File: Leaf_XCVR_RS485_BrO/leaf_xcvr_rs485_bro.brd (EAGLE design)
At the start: 22.5 x 31.7 mm, 11 parts, among them U1 RS485_XCVR_SN65HVD178X

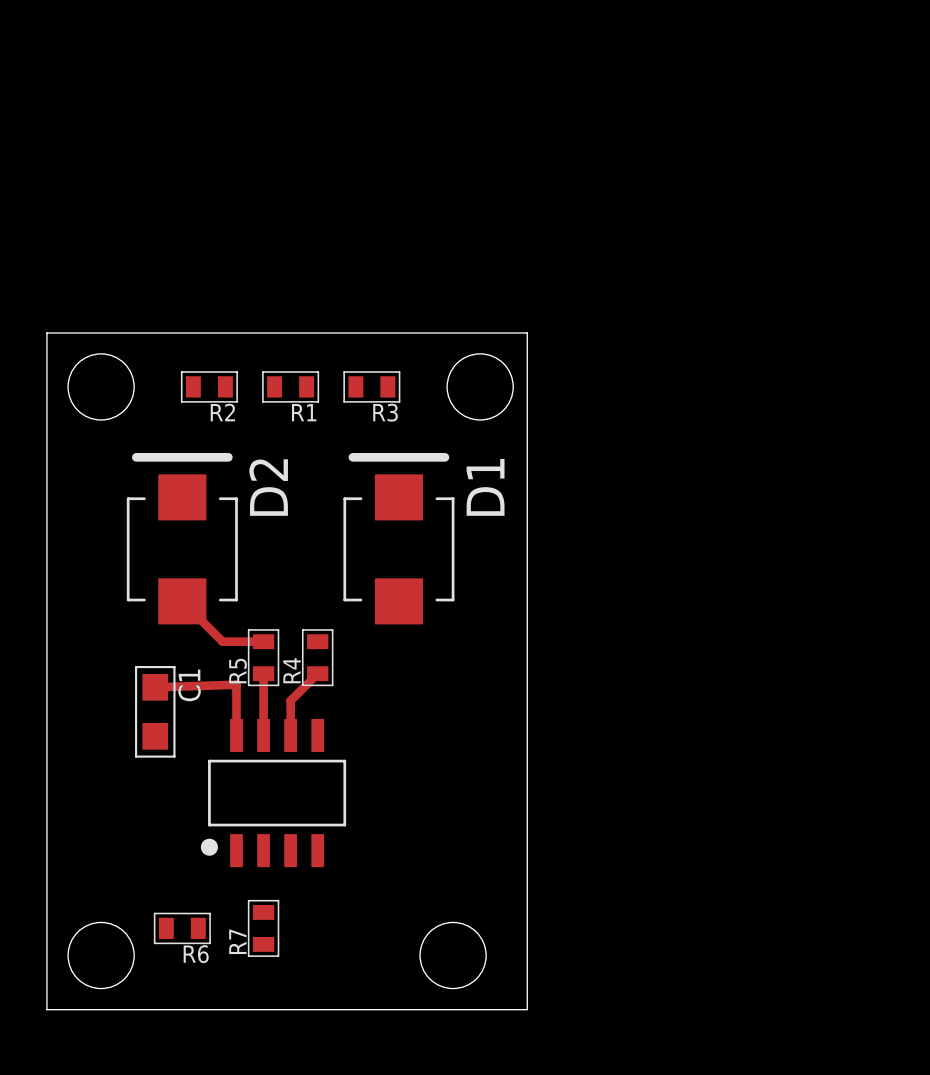
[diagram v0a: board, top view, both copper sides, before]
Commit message: new xcvr board for mockups
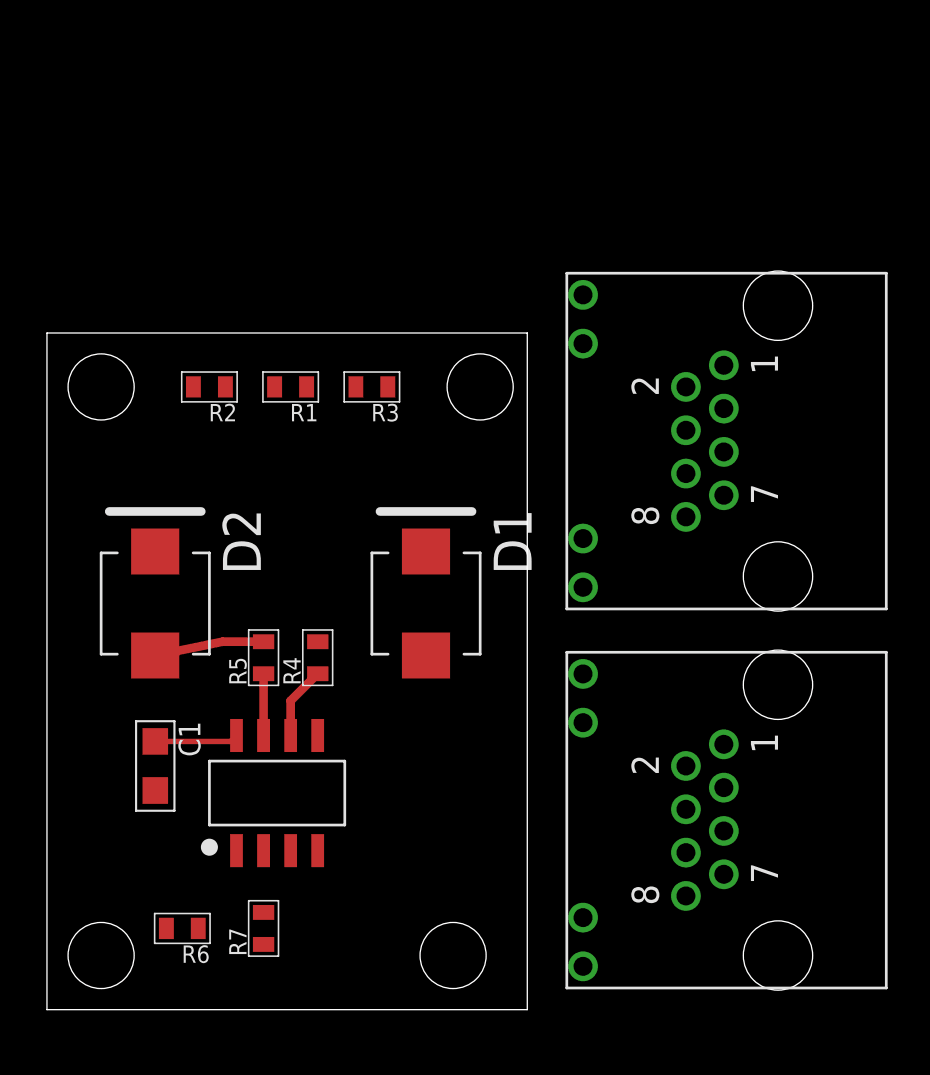
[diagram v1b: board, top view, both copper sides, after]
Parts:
- added J$1, J$2: (no value), stepOSP:RJHSE-5085
- moved D1 2.84 mm to (17.8, 19.1)
- moved D2 2.84 mm to (5.08, 19.1)
- moved C1 2.54 mm to (5.08, 11.4)
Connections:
- removed net N$3: C1.P$1, U1.8
- new net +3V3: C1.P$1, R2.P$2, R6.P$2, U1.8
- new net GND: C1.P$2, D1.P$1, D2.P$1, R3.P$1, R7.P$1, U1.5
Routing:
- net N$3: track 6.19 -> 0.00 mm
- net +3V3: track 0.00 -> 3.93 mm
- net N$7: track 4.59 -> 5.15 mm
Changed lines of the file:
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@@
 </autorouter>
 <elements>
-<element name="C1" library="stepOSP" package="0805" value="" x="5.08" y="13.97" rot="R270"/>
-<element name="D1" library="leaf" package="DO-214AA_LITTELFUSE" value="TVS_DO-214AA" x="16.51" y="21.59" rot="R270"/>
-<element name="D2" library="leaf" package="DO-214AA_LITTELFUSE" value="TVS_DO-214AA" x="6.35" y="21.59" rot="R270"/>
+<element name="C1" library="stepOSP" package="0805" value="" x="5.08" y="11.43" rot="R270"/>
+<element name="D1" library="leaf" package="DO-214AA_LITTELFUSE" value="TVS_DO-214AA" x="17.78" y="19.05" rot="R270"/>
+<element name="D2" library="leaf" package="DO-214AA_LITTELFUSE" value="TVS_DO-214AA" x="5.08" y="19.05" rot="R270"/>
 <element name="R1" library="stepOSP" package="0603" value="" x="11.43" y="29.21" rot="R180"/>
 <element name="R2" library="stepOSP" package="0603" value="" x="7.62" y="29.21" rot="R180"/>
@@
 <element name="R7" library="stepOSP" package="0603" value="" x="10.16" y="3.81" rot="R90"/>
 <element name="U1" library="leaf" package="SOIC_08_TI" value="RS485_XCVR_SN65HVD178X" x="8.89" y="10.16"/>
+<element name="J$1" library="stepOSP" package="RJHSE-5085" value="" x="34.29" y="2.54" rot="R90"/>
+<element name="J$2" library="stepOSP" package="RJHSE-5085" value="" x="34.29" y="20.32" rot="R90"/>
 </elements>
 <signals>
-<signal name="N$3">
-<contactref element="U1" pad="8"/>
-<contactref element="C1" pad="P$1"/>
-<wire x1="5.08" y1="15.12" x2="8.89" y2="15.24" width="0.4064" layer="1"/>
-<wire x1="8.89" y1="15.24" x2="8.89" y2="12.86" width="0.4064" layer="1"/>
-</signal>
 <signal name="N$1">
 <contactref element="U1" pad="6"/>
@@
 <wire x1="12.7" y1="17.26" x2="12.18" y2="29.21" width="0" layer="19" extent="1-1"/>
 <wire x1="14.49" y1="29.21" x2="12.7" y2="17.26" width="0" layer="19" extent="1-1"/>
-<wire x1="16.51" y1="19.1516" x2="14.49" y2="29.21" width="0" layer="19" extent="1-1"/>
+<wire x1="17.78" y1="16.6116" x2="14.49" y2="29.21" width="0" layer="19" extent="1-1"/>
 </signal>
 <signal name="N$7">
@@
 <contactref element="R2" pad="P$1"/>
 <wire x1="10.16" y1="17.26" x2="8.2416" y2="17.26" width="0.4064" layer="1"/>
-<wire x1="8.2416" y1="17.26" x2="6.35" y2="19.1516" width="0.4064" layer="1"/>
+<wire x1="8.2416" y1="17.26" x2="5.08" y2="16.6116" width="0.4064" layer="1"/>
 <wire x1="8.37" y1="29.21" x2="10.68" y2="29.21" width="0" layer="19" extent="1-1"/>
-<wire x1="6.35" y1="19.1516" x2="8.37" y2="29.21" width="0" layer="19" extent="1-1"/>
+<wire x1="5.08" y1="16.6116" x2="8.37" y2="29.21" width="0" layer="19" extent="1-1"/>
 </signal>
 <signal name="N$8">
@@
 <contactref element="U1" pad="4"/>
 </signal>
+<signal name="+3V3">
+<contactref element="R6" pad="P$2"/>
+<contactref element="R2" pad="P$2"/>
+<contactref element="C1" pad="P$1"/>
+<contactref element="U1" pad="8"/>
+<wire x1="5.08" y1="12.58" x2="8.61" y2="12.58" width="0.254" layer="1"/>
+<wire x1="8.61" y1="12.58" x2="8.89" y2="12.86" width="0.254" layer="1"/>
+<wire x1="8.89" y1="12.86" x2="6.87" y2="29.21" width="0" layer="19" extent="1-1"/>
+<wire x1="5.6" y1="3.81" x2="5.08" y2="12.58" width="0" layer="19" extent="1-1"/>
+</signal>
+<signal name="GND">
+<contactref element="C1" pad="P$2"/>
+<contactref element="D2" pad="P$1"/>
+<contactref element="D1" pad="P$1"/>
+<contactref element="R3" pad="P$1"/>
+<contactref element="R7" pad="P$1"/>
+<contactref element="U1" pad="5"/>
+<wire x1="17.78" y1="21.4884" x2="15.99" y2="29.21" width="0" layer="19" extent="1-1"/>
+<wire x1="5.08" y1="21.4884" x2="17.78" y2="21.4884" width="0" layer="19" extent="1-1"/>
+<wire x1="5.08" y1="10.28" x2="5.08" y2="21.4884" width="0" layer="19" extent="1-1"/>
+<wire x1="12.7" y1="12.86" x2="5.08" y2="10.28" width="0" layer="19" extent="1-1"/>
+<wire x1="10.16" y1="3.06" x2="12.7" y2="12.86" width="0" layer="19" extent="1-1"/>
+</signal>
 </signals>

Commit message: updating rs485 breakout
added a few new connectors and trying out some new designs
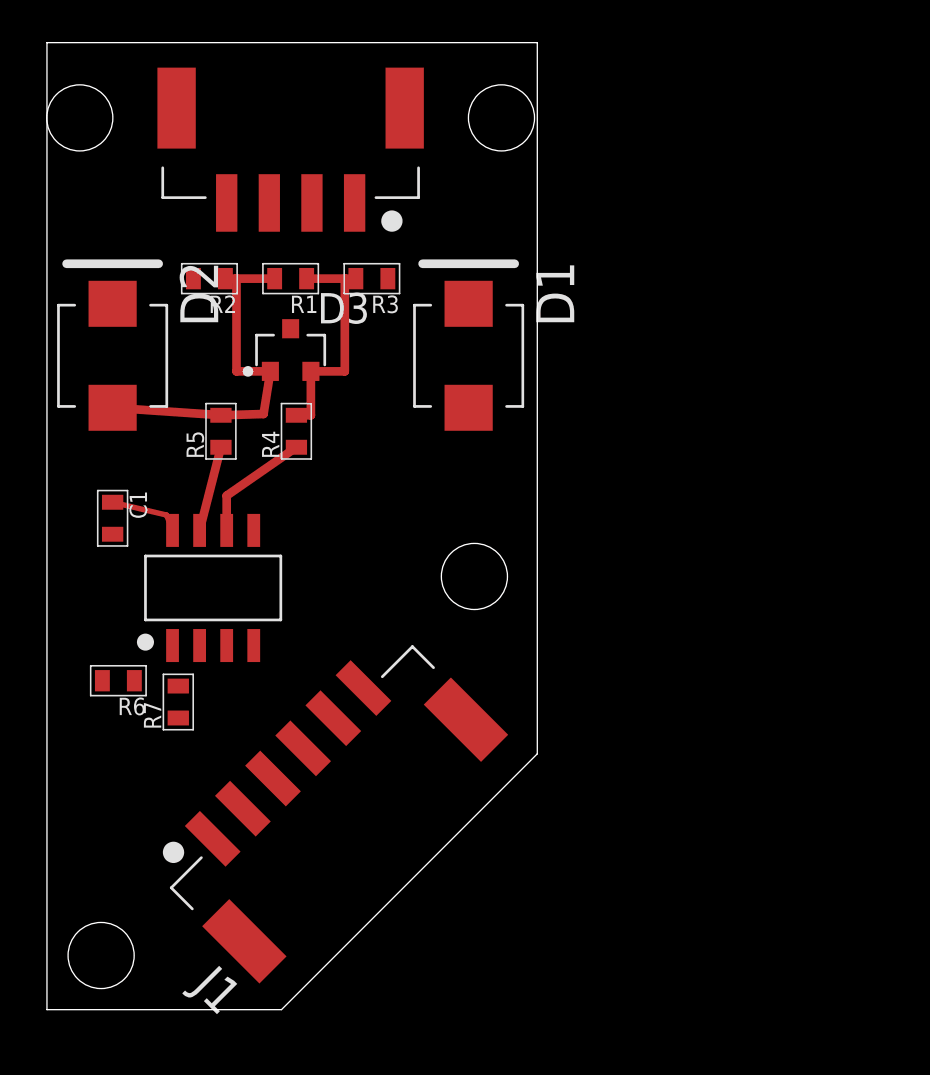
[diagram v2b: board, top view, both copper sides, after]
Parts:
- removed J$1, J$2: (no value), stepOSP:RJHSE-5085
- added D3: TVS_SOT-23, leaf:SOT-23_ONSEMI
- added J1: CONN_6X1_JST_PA, leaf:CONN_6X1_JST_PA
- added J2: CONN_4X1_JST_PA, leaf:CONN_4X1_JST_PA
- C1: device stepOSP:0805 -> stepOSP:0603
- moved R6 12.0 mm to (3.35, 15.4)
- moved C1 11.8 mm to (3.08, 23.1)
- moved D1 11.8 mm to (19.8, 30.7)
- moved D2 11.8 mm to (3.08, 30.7)
- moved R7 11.3 mm to (6.16, 14.4)
- moved R5 10.8 mm to (8.16, 27.1)
- moved R4 10.7 mm to (11.7, 27.1)
- moved U1 10.1 mm to (5.89, 19.8)
- moved R1 5.08 mm to (11.4, 34.3)
- moved R2 5.08 mm to (7.62, 34.3)
- moved R3 5.08 mm to (15.2, 34.3)
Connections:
- new net N$4: J1.2
- new net N$5: J2.4
- net +3V3: now also J1.3
- net GND: now also D3.3, J1.1, J2.1
- net N$10: now also J1.6
- net N$6: now also D3.2, J2.2
- net N$7: now also D3.1, J2.3
- net N$8: now also J1.5
- net N$9: now also J1.4
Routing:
- net N$7: track 5.15 -> 17.5 mm
- net N$6: track 0.00 -> 11.0 mm
- net N$1: track 3.43 -> 5.61 mm
- net N$2: track 2.90 -> 4.03 mm
- net +3V3: track 3.93 -> 3.37 mm
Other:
- board size 22.5 x 31.7 mm -> 23 x 45.4 mm

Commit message: latest and greatest
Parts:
- J1: value CONN_6X1_JST_PA -> CONN_7X1_JST_PA; device leaf:CONN_6X1_JST_PA -> leaf:CONN_7X1_JST_PA
- moved D3 7.69 mm to (16.9, 25.6), turned to 315 degrees
- moved R4 5.83 mm to (14.7, 22.1), turned to 45 degrees
- moved R5 5.83 mm to (13.2, 24.1), turned to 45 degrees
- moved R2 5.50 mm to (12.3, 31.4), turned to 90 degrees
- moved R1 5.00 mm to (14.4, 30.3)
- moved D2 4.47 mm to (7.08, 28.7)
- moved C1 4.12 mm to (7.08, 22.1), turned to 225 degrees
- moved R3 3.39 mm to (16.7, 31.2), turned to 270 degrees
- moved U1 2.91 mm to (8.78, 20.1), turned to 315 degrees
- moved J1 2.40 mm to (20.0, 6.00)
- moved D1 2.24 mm to (21.8, 29.7)
- moved R6 2.24 mm to (4.35, 17.4), turned to 135 degrees
- moved J2 1.58 mm to (13.0, 46.8)
- moved R7 1.00 mm to (7.16, 14.4), turned to 135 degrees
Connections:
- removed net GND: C1.P$2, D1.P$1, D2.P$1, D3.3, J1.1, J2.1, R3.P$1, R7.P$1, U1.5
- removed net N$4: J1.2
- removed net N$5: J2.4
- new net GND1: C1.P$2, D1.P$1, D2.P$1, D3.3, J1.3, R3.P$1, R7.P$1, U1.5
- new net GND2: J1.1, J2.1
- new net V+: J1.2, J2.4
- net +3V3: now also J1.4; no longer J1.3
- net N$10: now also J1.7; no longer J1.6
- net N$8: now also J1.6; no longer J1.5
- net N$9: now also J1.5; no longer J1.4
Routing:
- net N$7: track 17.5 -> 0.00 mm
- net N$6: track 11.0 -> 0.00 mm
- net N$1: track 5.61 -> 0.00 mm
- net N$2: track 4.03 -> 0.00 mm
- net +3V3: track 3.37 -> 0.00 mm
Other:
- board size 23 x 45.4 mm -> 26 x 45 mm

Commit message: submission to OSHpark
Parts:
- added TP1, TP2, TP3, TP4, TP5, TP6, TP7, TP8, TP9: TP1, leaf:TP1
- added U$1: STEPS_LOGO, stepOSP:STEPS_LOGO
- C1: value (none) -> 0.1u
- R1: value (none) -> 120
- R4, R5: value (none) -> 10
- R6, R7: value (none) -> 3.3k
- moved D1 16.6 mm to (5.33, 27.8), turned to 0 degrees
- moved D2 6.82 mm to (5.33, 22.1), turned to 0 degrees
- moved J2 6.50 mm to (13.0, 40.3)
- moved R1 6.17 mm to (12.6, 24.4), turned to 225 degrees
- moved R2 5.77 mm to (11.3, 25.7), turned to 225 degrees
- moved C1 5.15 mm to (4.58, 17.6)
- moved R6 4.59 mm to (2.75, 13.1)
- moved D3 4.47 mm to (14.9, 21.6)
- moved U1 4.47 mm to (6.78, 16.1)
- moved R5 4.27 mm to (11.7, 20.1)
- moved R4 4.21 mm to (13.4, 18.1)
- moved R7 4.13 mm to (4.96, 10.9)
- moved R3 3.71 mm to (15.3, 27.8), turned to 180 degrees
- moved J1 0.71 mm to (20.5, 5.50)
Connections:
- net +3V3: now also J1.5, TP6.P$1; no longer J1.4
- net GND1: now also D1.1, D2.1, J1.1, TP9.P$1; no longer D1.P$1, D2.P$1, J1.3
- net GND2: now also J1.7, TP8.P$1; no longer J1.1
- net N$10: now also J1.2, TP3.P$1; no longer J1.7
- net N$6: now also D1.2, TP2.P$1; no longer D1.P$2
- net N$7: now also D2.2, TP1.P$1; no longer D2.P$2
- net N$8: now also J1.3, TP5.P$1; no longer J1.6
- net N$9: now also J1.4, TP4.P$1; no longer J1.5
- net V+: now also J1.6, TP7.P$1; no longer J1.2
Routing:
- net N$6: track 0.00 -> 39.1 mm, vias 0 -> 1
- net +3V3: track 0.00 -> 36.9 mm, vias 0 -> 2
- net V+: track 0.00 -> 31.5 mm, vias 0 -> 2
- net N$7: track 0.00 -> 26.6 mm, vias 0 -> 3
- net GND2: track 0.00 -> 19.1 mm, vias 0 -> 2
- net N$9: track 0.00 -> 17.6 mm, vias 0 -> 1
- net N$8: track 0.00 -> 16.4 mm, vias 0 -> 1
- net N$10: track 0.00 -> 11.0 mm, vias 0 -> 1
- net N$2: track 0.00 -> 3.12 mm
- net N$1: track 0.00 -> 2.95 mm
- added copper zone on layer 1, net GND1
- added copper zone on layer 16, net GND1
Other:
- board size 26 x 45 mm -> 26 x 38.5 mm
- board text added: "Project Leaf"
- board text added: "REV A1"
- board text added: "RS485"
